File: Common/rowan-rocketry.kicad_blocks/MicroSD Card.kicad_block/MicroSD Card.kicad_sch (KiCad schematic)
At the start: 2 parts, among them J1 Micro_SD_Card

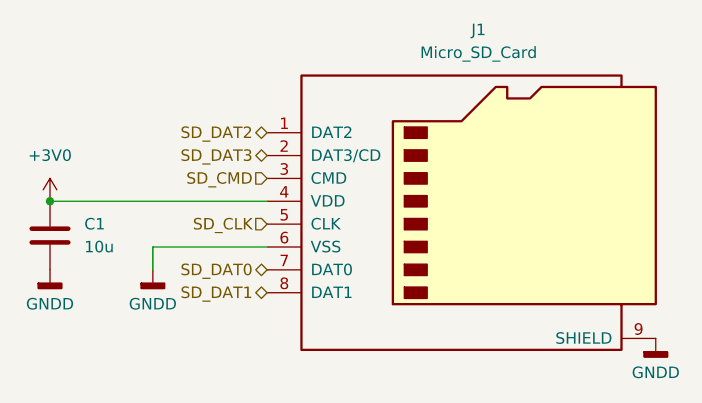
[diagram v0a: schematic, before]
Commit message: More reuse blocks. Added battery circuit to ride along board
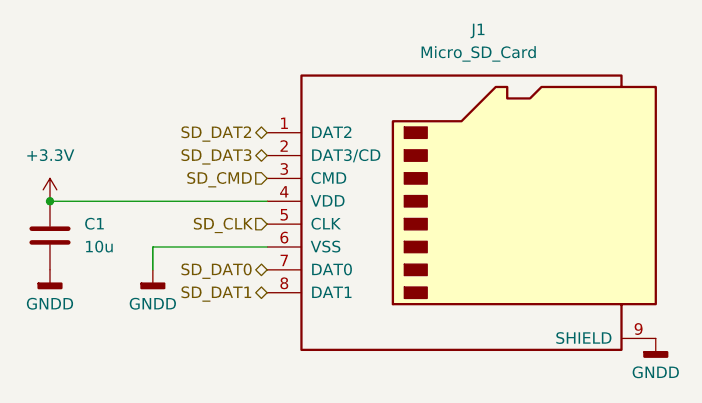
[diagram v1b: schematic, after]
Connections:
- net +3V0 renamed +3.3V
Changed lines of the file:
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@@
+	)
+	(symbol
+		(lib_id "power:+3.3V")
+		(at 101.6 87.63 0)
+		(unit 1)
+		(exclude_from_sim no)
+		(in_bom yes)
+		(on_board yes)
+		(dnp no)
+		(fields_autoplaced yes)
+		(property "Reference" "#PWR02"
+			(at 101.6 91.44 0)
+			(effects
+				(font
+					(size 1.27 1.27)
+				)
+				(hide yes)
+			)
+		)
+		(property "Value" "+3.3V"
+			(at 101.6 82.55 0)
+			(effects
+				(font
+					(size 1.27 1.27)
+				)
+			)
+		)
+		(property "Footprint" ""
+			(at 101.6 87.63 0)
+			(effects
+				(font
+					(size 1.27 1.27)
+				)
+				(hide yes)
+			)
+		)
+		(property "Datasheet" ""
+			(at 101.6 87.63 0)
+			(effects
+				(font
+					(size 1.27 1.27)
+				)
+				(hide yes)
+			)
+		)
+		(property "Description" "Power symbol creates a global label with name \"+3.3V\""
+			(at 101.6 87.63 0)
+			(effects
+				(font
+					(size 1.27 1.27)
+				)
+				(hide yes)
+			)
+		)
+		(pin "1"
+		)
+		(instances
+			(project ""
+				(path "/7761db1c-f9c0-4350-aff2-01ef05a45511"
+					(reference "#PWR02")
+					(unit 1)
+				)
+			)
+		)
 	)
 	(symbol
@@
 					(unit 1)
 				)
-			)
-		)
-	)
-	(symbol
-		(lib_id "power:+3V0")
-		(at 101.6 87.63 0)
-		(unit 1)
-		(exclude_from_sim no)
-		(in_bom yes)
-		(on_board yes)
-		(dnp no)
-		(fields_autoplaced yes)
-		(property "Reference" "#PWR02"
-			(at 101.6 91.44 0)
-			(effects
-				(font
-					(size 1.27 1.27)
-				)
-				(hide yes)
-			)
-		)
-		(property "Value" "+3V0"
-			(at 101.6 82.55 0)
-			(effects
-				(font
-					(size 1.27 1.27)
-				)
-			)
-		)
-		(property "Footprint" ""
-			(at 101.6 87.63 0)
-			(effects
-				(font
-					(size 1.27 1.27)
-				)
-				(hide yes)
-			)
-		)
-		(property "Datasheet" ""
-			(at 101.6 87.63 0)
-			(effects
-				(font
-					(size 1.27 1.27)
-				)
-				(hide yes)
-			)
-		)
-		(property "Description" "Power symbol creates a global label with name \"+3V0\""
-			(at 101.6 87.63 0)
-			(effects
-				(font
-					(size 1.27 1.27)
-				)
-				(hide yes)
-			)
-		)
-		(pin "1"
-		)
-		(instances
-			(project ""
-				(path "/7761db1c-f9c0-4350-aff2-01ef05a45511"
-					(reference "#PWR02")
-					(unit 1)
-				)
